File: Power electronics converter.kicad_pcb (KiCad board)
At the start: 2 copper layers, 112.6 x 69.1 mm, 85 parts, among them IC1 LM66200DRLR, J1 USB_B_Micro, J2 Conn_01x04_Pin, J3 Conn_01x04_Pin, J4 Conn_01x04_Pin, Q1 BSC082N10LSG, Q2 BSC082N10LSG, SW1 SW_SPDT, U1 STM32F103CBTx, U2 IRS2186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

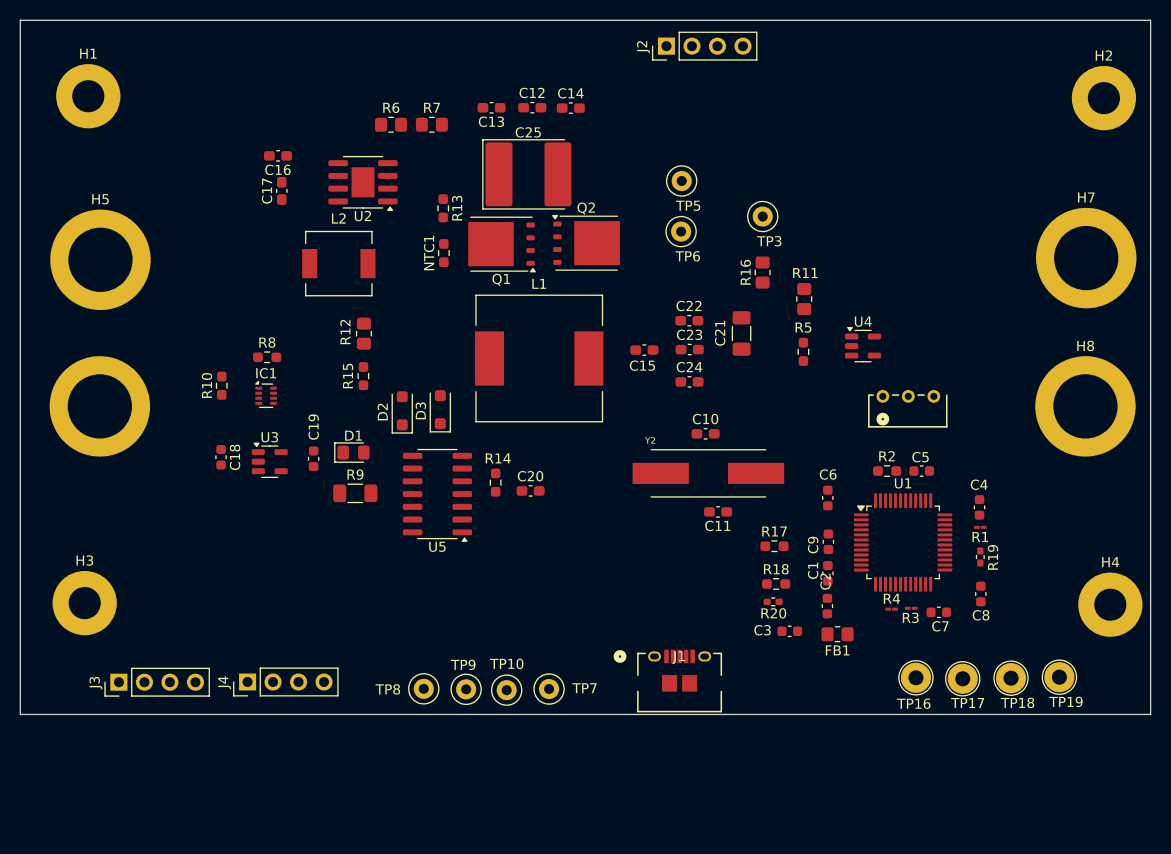
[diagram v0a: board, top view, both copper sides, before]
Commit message: Placement finished routing started
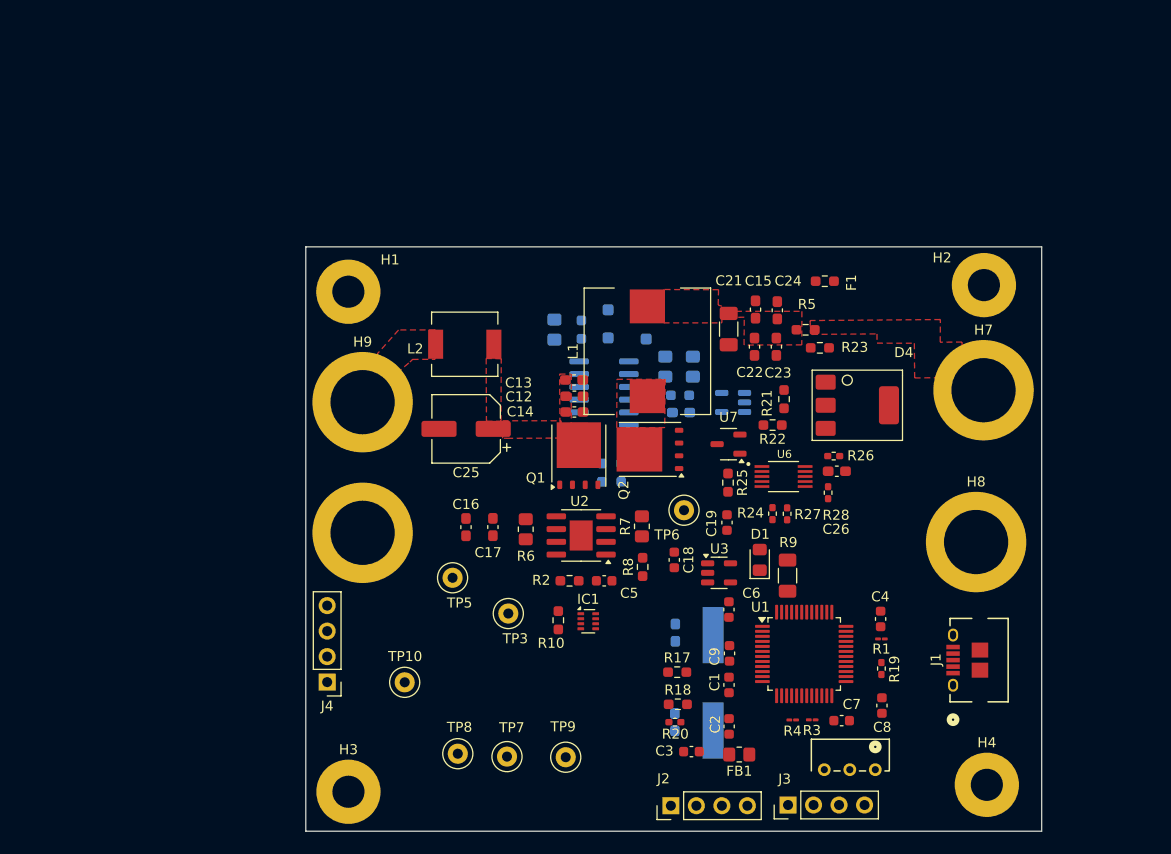
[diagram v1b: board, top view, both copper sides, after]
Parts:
- removed TP16, TP17, TP18, TP19: TestPoint, TestPoint:TestPoint_Loop_D2.54mm_Drill1.5mm_Beaded
- added C26: 0.1uF, Capacitor_SMD:C_0603_1608Metric_Pad1.08x0.95mm_HandSolder, F.Cu at (119.1, 97.9)
- added D4: Q_SCR_KAG, Library:NYC222_THYRISTOR_FOOTPRINT, F.Cu at (121.1, 91.3)
- added F1: Fuse, Resistor_SMD:R_0603_1608Metric_Pad0.98x0.95mm_HandSolder, F.Cu at (117.9, 78.9)
- added R21: 11k, Resistor_SMD:R_0603_1608Metric_Pad0.98x0.95mm_HandSolder, F.Cu at (113.8, 90.7)
- added R22: 10k, Resistor_SMD:R_0603_1608Metric_Pad0.98x0.95mm_HandSolder, F.Cu at (112.7, 93.3)
- added R23: 2.7k, Resistor_SMD:R_0603_1608Metric_Pad0.98x0.95mm_HandSolder, F.Cu at (117.4, 85.6)
- added R24: 10k, Resistor_SMD:R_0402_1005Metric_Pad0.72x0.64mm_HandSolder, F.Cu at (112.7, 102.1)
- added R25: 27.1, Resistor_SMD:R_0603_1608Metric_Pad0.98x0.95mm_HandSolder, F.Cu at (108.2, 99.0)
- added R26: 200, Resistor_SMD:R_0402_1005Metric_Pad0.72x0.64mm_HandSolder, F.Cu at (118.7, 96.3)
- added R27: 10k, Resistor_SMD:R_0402_1005Metric_Pad0.72x0.64mm_HandSolder, F.Cu at (114.1, 102.1)
- added R28: 10k, Resistor_SMD:R_0402_1005Metric_Pad0.72x0.64mm_HandSolder, F.Cu at (118.2, 100.0)
- added U6: INA300AIDGSR, Library:SOP50P490X110-10N-INA300, F.Cu at (113.8, 98.4)
- added U7: TL431D, Library:LM431, F.Cu at (108.3, 95.2)
- C10, C11, C20, D2, D3, NTC1, R11, R12, R13, R14, R15, R16, U4, U5, Y2: moved to B.Cu
- C25: footprint Capacitor_Tantalum_SMD:CP_EIA-7260-20_AVX-M_HandSolder -> Capacitor_SMD:CP_Elec_6.3x5.7
- L1: value 15 uH -> 22 uH; footprint Inductor_SMD:L_12x12mm_H8mm -> Library:INDUCTOR_TDK_BUCK
- moved SW1 86.7 mm to (83.5, 126.3), turned to 180 degrees
- moved J2 75.7 mm to (102.5, 131.2)
- moved J3 67.8 mm to (114.2, 131.1)
- moved TP3 47.0 mm to (86.3, 112.0)
- moved C18 46.3 mm to (102.9, 106.7)
- moved U3 46.1 mm to (107.3, 108.0)
- moved TP5 45.6 mm to (80.8, 108.5)
- moved R7 45.1 mm to (99.6, 103.3), turned to 90 degrees
- moved R9 43.8 mm to (114.2, 108.3), turned to -90 degrees
- moved R8 42.8 mm to (99.7, 107.4), turned to 90 degrees
- moved R6 42.5 mm to (88.1, 103.6), turned to 90 degrees
- moved D1 41.8 mm to (111.4, 106.7), turned to 90 degrees
- moved C19 41.7 mm to (108.1, 103.0), turned to 90 degrees
- moved C16 41.4 mm to (82.1, 103.4), turned to -90 degrees
- moved U2 41.3 mm to (93.6, 104.3)
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- renumbered H5 to H9
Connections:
- net +3V3A renamed Net-(U1-VDDA)
- H7 pad 1: /Connectors/VOUT -> VOUT
- U1 pad 26: unconnected-(U1-PB13-Pad26) -> ALERT
- U1 pad 27: unconnected-(U1-PB14-Pad27) -> ENABLE
- U1 pad 28: unconnected-(U1-PB15-Pad28) -> LATCH
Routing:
- added copper zone on F.Cu, net /Power Stage Section/SW_NODE
- added copper zone on F.Cu, net INPUT POWER
- added copper zone on F.Cu, net VIN
- added copper zone on F.Cu, net VOUT
- added copper zone on F.Cu, net VSHUNT_PLUS
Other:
- board size 112.6 x 69.1 mm -> 73.3 x 58.2 mm

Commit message: Power loop routed
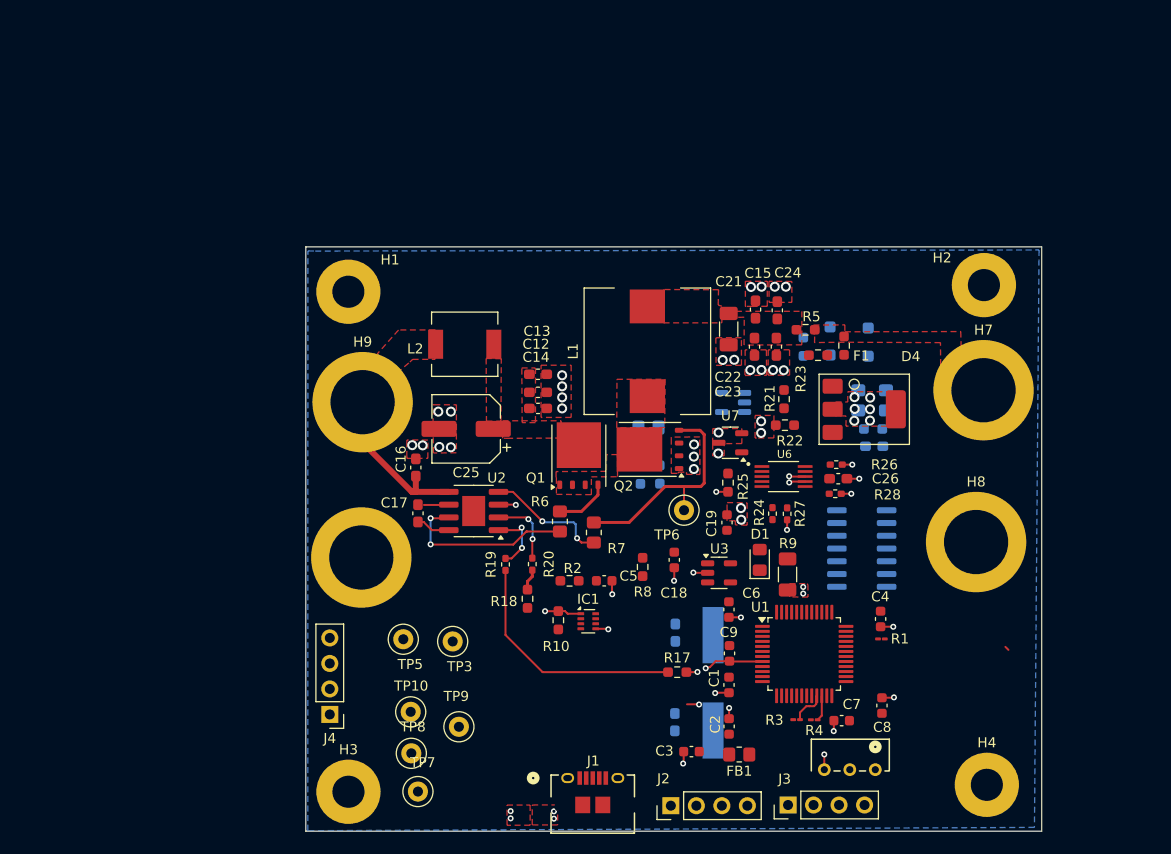
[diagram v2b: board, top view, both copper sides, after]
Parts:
- moved J1 41.1 mm to (94.8, 131.0), turned to 0 degrees
- moved R19 38.8 mm to (86.1, 107.1), turned to 90 degrees
- moved U5 29.6 mm to (121.5, 105.6)
- moved D2 22.2 mm to (122.2, 85.0)
- moved D3 22.2 mm to (118.4, 84.9)
- moved R15 22.2 mm to (115.7, 85.5)
- moved R20 21.2 mm to (88.7, 107.1), turned to 90 degrees
- moved C20 19.5 mm to (122.8, 95.4)
- moved R11 19.5 mm to (124.0, 90.8)
- moved R14 19.5 mm to (122.7, 93.7)
- moved R16 19.5 mm to (121.2, 90.8)
- moved R18 18.3 mm to (88.3, 110.6), turned to -90 degrees
- moved R12 13.5 mm to (100.3, 93.5), turned to 180 degrees
- moved TP9 11.1 mm to (81.4, 123.3)
- moved U2 11.0 mm to (82.9, 101.8)
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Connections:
- C18 pad 2: SGND -> GND
- C19 pad 2: SGND -> GND
- R17 pad 2: SGND -> GND
- R18 pad 2: SGND -> GND
- R9 pad 2: SGND -> GND
- U3 pad 2: SGND -> GND
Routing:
- net GND: track 0.00 -> 38.0 mm, vias 0 -> 65
- net HIGH_SIDE_PWM: track 0.00 -> 24.2 mm
- net GATE_LS: track 0.00 -> 22.5 mm
- net Net-(U2-HO): track 0.00 -> 17.9 mm, vias 0 -> 2
- net INPUT POWER: track 0.00 -> 16.2 mm
- net Net-(U2-LO): track 0.00 -> 12.3 mm, vias 0 -> 2
- net Net-(U2-LIN): track 0.00 -> 7.12 mm, vias 0 -> 2
- net Net-(U2-HIN): track 0.00 -> 6.52 mm, vias 0 -> 2
- net GATE_HS: track 0.00 -> 5.50 mm
- net /MCU Section/I2C_SCL: track 0.00 -> 3.54 mm
- net Net-(U2-VB): track 0.00 -> 3.41 mm
- net /MCU Section/I2C_SDA: track 0.00 -> 2.56 mm
- net Net-(U2-VS): track 0.00 -> 2.49 mm
- net LOW_SIDE_PWM: track 0.00 -> 2.14 mm
- added copper zone on B.Cu, net GND
- added copper zone on F.Cu, net GND

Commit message: Most of sensing routed
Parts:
- removed TP10, TP3, TP5, TP7, TP8, TP9: TestPoint, TestPoint:TestPoint_Loop_D2.50mm_Drill1.0mm
- R11, R16: moved to F.Cu
- moved SW1 38.8 mm to (46.1, 116.3)
- moved C20 18.4 mm to (105.0, 90.5), turned to -90 degrees
- moved R14 17.6 mm to (106.0, 88.0)
- moved R16 12.8 mm to (125.8, 102.8), turned to -90 degrees
- moved U5 9.91 mm to (113.9, 99.2), turned to 0 degrees
- moved R11 8.15 mm to (125.8, 98.8)
- moved R8 5.90 mm to (98.7, 113.2)
- moved C19 0.92 mm to (107.2, 103.0)
- moved R12 0.71 mm to (99.6, 93.6), turned to 0 degrees
- moved U1 0.48 mm to (116.2, 116.2)
- moved D4 0.32 mm to (121.8, 92.0)
- moved U4 0.26 mm to (108.7, 90.8)
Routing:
- net Net-(D4-G): track 0.00 -> 18.8 mm
- net /ADC sensing/I_OUT_SENSING: track 0.00 -> 18.5 mm, vias 0 -> 2
- net USB POWER: track 0.00 -> 18.4 mm, vias 0 -> 2
- net Net-(SW1-B): track 0.00 -> 17.7 mm, vias 0 -> 2
- net /ADC sensing/VIN_SENSING: track 0.00 -> 17.6 mm, vias 0 -> 2
- net /ADC sensing/T_SENSING: track 0.00 -> 15.6 mm, vias 0 -> 2
- net VOUT: track 0.00 -> 15.2 mm, vias 0 -> 1
- net +5VBUS: track 0.00 -> 12.4 mm, vias 0 -> 2
- net VSHUNT_PLUS: track 0.00 -> 11.9 mm, vias 0 -> 1
- net VIN: track 0.00 -> 8.83 mm, vias 0 -> 1
- net INPUT POWER: track 16.2 -> 23.0 mm, vias 0 -> 2
- net Net-(R14-Pad1): track 0.00 -> 6.66 mm, vias 0 -> 2
- net Net-(D4-K): track 0.00 -> 5.21 mm
- net Net-(IC1-ST): track 0.00 -> 4.21 mm
- net Net-(IC1-ON): track 0.00 -> 2.27 mm
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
